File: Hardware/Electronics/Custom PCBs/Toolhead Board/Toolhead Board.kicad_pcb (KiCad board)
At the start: 4 copper layers, 75 x 75 mm, 161 parts, among them J1 USB C Receptacle, J2 Conn_02x04_Odd_Even, J3 Conn_02x08_Odd_Even, J4 Conn_02x08_Odd_Even, J5 Conn_02x08_Odd_Even, J6 Conn_02x04_Odd_Even, J7 Conn_01x02, J8 Conn_01x02, J9 120TR, Q1 MMBT4403, Q2 MMBT4403, Q3 MMBT4403, SW1 BOOT, SW2 RESET, U1 LF15_TO220, U10 BMI270, U11 G20N06D52, U12 G20N06D52, U13 PCA9685BS, U2 LF15_TO220, U3 RP2040, U4 W25Q128JVS, U5 SN65HVD1050D, U6 TMC2209-LA, U7 HX711, U8 HX711, U9 HX711, Y1 12MHz/12pF/50Ω/20ppm

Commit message: Update base mounting
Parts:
- C16: moved to B.Cu
- moved C5 99.6 mm to (75.2, 120.5), turned to -90 degrees
- moved C8 98.8 mm to (71.5, 122.9)
- moved C7 95.5 mm to (72.1, 116.0)
- moved C10 95.0 mm to (81.4, 118.3)
- moved C11 95.0 mm to (81.4, 120.8)
- moved C12 95.0 mm to (81.4, 123.3)
- moved C13 95.0 mm to (85.7, 115.8)
- moved C14 95.0 mm to (85.7, 118.3)
- moved C15 95.0 mm to (85.7, 120.8)
- moved C9 95.0 mm to (81.4, 115.8)
- moved C6 93.8 mm to (76.3, 115.8)
- moved C20 92.4 mm to (66.4, 99.8), turned to -90 degrees
- moved C19 92.1 mm to (67.9, 99.8), turned to -90 degrees
- moved C2 87.8 mm to (46.0, 43.4)
- moved C3 87.8 mm to (46.0, 45.9)
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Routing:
- net GNDA: track 278.8 -> 145.2 mm
- net D7: track 0.00 -> 26.9 mm
- net D0: track 0.00 -> 25.6 mm
- net D8: track 0.00 -> 24.9 mm
- net D1: track 0.00 -> 23.0 mm
- net SCL: track 1.94 -> 24.1 mm
- net SDA: track 1.61 -> 21.7 mm
- net /Microcontroller/RUN: track 0.00 -> 12.0 mm, vias 0 -> 2
- net +3.3V: track 66.9 -> 73.6 mm
- net V_MOT: track 40.1 -> 43.0 mm
- net MOT_DIAG: track 20.7 -> 21.0 mm, vias 1 -> 0

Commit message: Update layout slightly
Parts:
- C23, CR1: moved to B.Cu
- J7: footprint Connector_JST:JST_XH_B2B-XH-AM_1x02_P2.50mm_Vertical -> Connector_JST:JST_PH_B2B-PH-K_1x02_P2.00mm_Vertical
- J8: footprint Connector_JST:JST_XH_B2B-XH-AM_1x02_P2.50mm_Vertical -> Connector_AMASS:AMASS_XT30U-F_1x02_P5.0mm_Vertical
- moved C26 54.4 mm to (99.7, 58.0), turned to -120 degrees
- moved R10 49.0 mm to (33.9, 72.4), turned to 0 degrees
- moved C23 47.7 mm to (34.4, 68.9), turned to -90 degrees
- moved U5 42.0 mm to (45.6, 69.0), turned to 168.5 degrees
- moved J8 12.7 mm to (45.7, 58.2), turned to -60 degrees
- moved CR1 11.2 mm to (46.1, 69.1), turned to -11.5 degrees
- moved C1 11.0 mm to (37.0, 65.3)
- moved R11 9.68 mm to (39.6, 56.4)
- moved TP5 8.59 mm to (117.5, 62.1)
- moved J9 8.21 mm to (37.2, 60.5)
- moved J7 2.41 mm to (40.9, 67.0), turned to -101.5 degrees
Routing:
- net V_MOT: track 43.0 -> 18.6 mm
- net CAN_H: track 19.6 -> 0.00 mm, vias 2 -> 1
- net STRAIN_SCK: track 0.00 -> 19.4 mm, vias 0 -> 2
- net +5V: track 14.2 -> 31.9 mm
- net +3.3V: track 73.6 -> 90.8 mm
- net CAN_RX: track 8.87 -> 0.00 mm
- net CAN_L: track 7.56 -> 0.00 mm
- net CAN_S: track 4.37 -> 0.00 mm, vias 1 -> 0
- net CAN_TX: track 4.32 -> 0.00 mm
- net Net-(J9-Pin_1): track 2.44 -> 0.00 mm
- net Net-(U5-VREF): track 1.56 -> 0.00 mm
- net Net-(U5-S): vias 1 -> 0

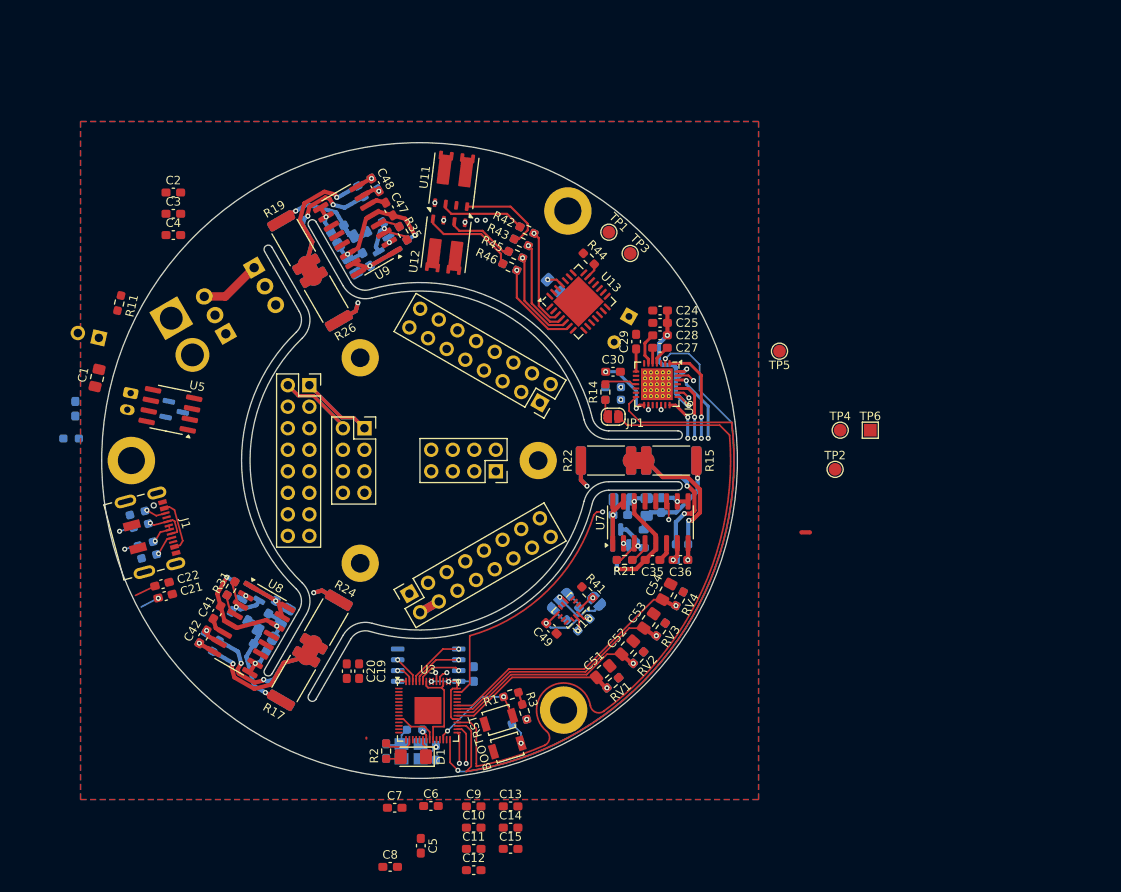
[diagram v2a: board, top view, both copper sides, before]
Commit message: Update toolhead schematic+layout and add tolerances to base
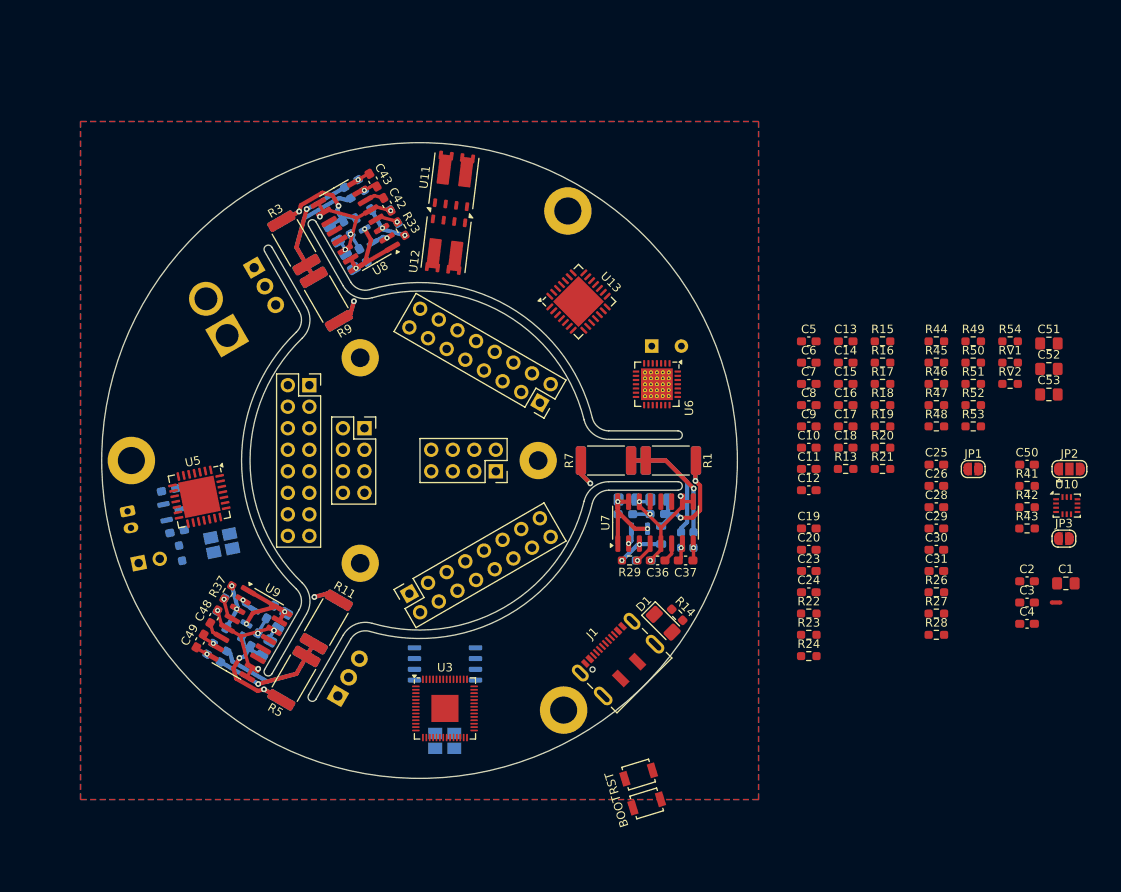
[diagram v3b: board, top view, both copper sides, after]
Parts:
- removed C54: 10u, Capacitor_SMD:C_0805_2012Metric_Pad1.18x1.45mm_HandSolder
- removed RV3, RV4: CG0603MLC-3.3LE, Resistor_SMD:R_0603_1608Metric_Pad0.98x0.95mm_HandSolder
- removed TP1, TP2, TP3, TP4, TP5: TestPoint, TestPoint:TestPoint_Pad_D1.5mm
- removed TP6: TestPoint, TestPoint:TestPoint_Pad_1.5x1.5mm
- added Y2: 16MHz/12pF, Oscillator:Oscillator_SMD_SeikoEpson_SG210-4Pin_2.5x2.0mm_HandSoldering, B.Cu at (51.7, 84.7)
- C16, C17, C18, JP2, JP3, R49, R50, R53, R54: moved to F.Cu
- C19: value 1u -> 100n
- C21, C22, C35, C41, C47: moved to B.Cu
- C23: value 100n -> 22p; moved to F.Cu
- C24: value 100n -> 22p
- C26: value 100u -> 100n; footprint Capacitor_THT:CP_Radial_D8.0mm_P3.50mm -> Capacitor_SMD:C_0603_1608Metric_Pad1.08x0.95mm_HandSolder; moved to F.Cu
- C27: value 22n -> 100u; footprint Capacitor_SMD:C_0603_1608Metric_Pad1.08x0.95mm_HandSolder -> Capacitor_THT:CP_Radial_D8.0mm_P3.50mm; moved to B.Cu
- C28: value 100n -> 22n
- C29: value 4.7u -> 100n
- C30: value 100n -> 4.7u
- C31: value 10uF -> 100n; footprint Capacitor_SMD:C_0805_2012Metric_Pad1.18x1.45mm_HandSolder -> Capacitor_SMD:C_0603_1608Metric_Pad1.08x0.95mm_HandSolder; moved to F.Cu
- C32, C34, C38, C40, C44, C46: value 0.1uF -> 10uF; footprint Capacitor_SMD:C_0603_1608Metric_Pad1.08x0.95mm_HandSolder -> Capacitor_SMD:C_0805_2012Metric_Pad1.18x1.45mm_HandSolder
- C33, C39, C45: value 10uF -> 0.1uF; footprint Capacitor_SMD:C_0805_2012Metric_Pad1.18x1.45mm_HandSolder -> Capacitor_SMD:C_0603_1608Metric_Pad1.08x0.95mm_HandSolder
- C37, C43: value 10uF -> 0.1uF; footprint Capacitor_SMD:C_0805_2012Metric_Pad1.18x1.45mm_HandSolder -> Capacitor_SMD:C_0603_1608Metric_Pad1.08x0.95mm_HandSolder; moved to F.Cu
- C49: value 100n -> 0.1uF
- C50: value 10u -> 100n; footprint Capacitor_SMD:C_0805_2012Metric_Pad1.18x1.45mm_HandSolder -> Capacitor_SMD:C_0603_1608Metric_Pad1.08x0.95mm_HandSolder; moved to F.Cu
- J8: footprint Connector_AMASS:AMASS_XT30U-F_1x02_P5.0mm_Vertical -> Connector_PinHeader_2.54mm:PinHeader_1x02_P2.54mm_Vertical
- J9: value 120TR -> Conn_01x02; footprint Connector_PinHeader_2.54mm:PinHeader_1x02_P2.54mm_Vertical -> Connector_AMASS:AMASS_XT30U-F_1x02_P5.0mm_Vertical
- R1, R3: value 10k -> 330; footprint Resistor_SMD:R_0603_1608Metric_Pad0.98x0.95mm_HandSolder -> Resistor_SMD:R_2512_6332Metric
- R10: value NC -> 330; footprint Resistor_SMD:R_0603_1608Metric_Pad0.98x0.95mm_HandSolder -> Resistor_SMD:R_2512_6332Metric
- R11: value 120 -> 330; footprint Resistor_SMD:R_0603_1608Metric_Pad0.98x0.95mm_HandSolder -> Resistor_SMD:R_2512_6332Metric
- R12: value 0R11 -> 330; footprint Resistor_SMD:R_0603_1608Metric_Pad0.98x0.95mm_HandSolder -> Resistor_SMD:R_2512_6332Metric
- R13: value 0R11 -> 10k; moved to F.Cu
- R14, R43, R46: value 100 -> 10k
- R15, R22, R24: value 330 -> 10k; footprint Resistor_SMD:R_2512_6332Metric -> Resistor_SMD:R_0603_1608Metric_Pad0.98x0.95mm_HandSolder
- R16: value 330 -> 1k; footprint Resistor_SMD:R_2512_6332Metric -> Resistor_SMD:R_0603_1608Metric_Pad0.98x0.95mm_HandSolder; moved to F.Cu
- R17: value 330 -> 1k; footprint Resistor_SMD:R_2512_6332Metric -> Resistor_SMD:R_0603_1608Metric_Pad0.98x0.95mm_HandSolder
- R18: value 330 -> 5.1k; footprint Resistor_SMD:R_2512_6332Metric -> Resistor_SMD:R_0603_1608Metric_Pad0.98x0.95mm_HandSolder; moved to F.Cu
- R19: value 330 -> 5.1k; footprint Resistor_SMD:R_2512_6332Metric -> Resistor_SMD:R_0603_1608Metric_Pad0.98x0.95mm_HandSolder
- R2: value 10k -> 330; footprint Resistor_SMD:R_0603_1608Metric_Pad0.98x0.95mm_HandSolder -> Resistor_SMD:R_2512_6332Metric; moved to B.Cu
- R20: value 330 -> 27.4; footprint Resistor_SMD:R_2512_6332Metric -> Resistor_SMD:R_0603_1608Metric_Pad0.98x0.95mm_HandSolder; moved to F.Cu
- R21: value 10k -> 27.4
- R23: value 330 -> 10k; footprint Resistor_SMD:R_2512_6332Metric -> Resistor_SMD:R_0603_1608Metric_Pad0.98x0.95mm_HandSolder; moved to F.Cu
- R25: value 330 -> 120; footprint Resistor_SMD:R_2512_6332Metric -> Resistor_SMD:R_0603_1608Metric_Pad0.98x0.95mm_HandSolder
- R26: value 330 -> 0R11; footprint Resistor_SMD:R_2512_6332Metric -> Resistor_SMD:R_0603_1608Metric_Pad0.98x0.95mm_HandSolder
- R27: value 330 -> 0R11; footprint Resistor_SMD:R_2512_6332Metric -> Resistor_SMD:R_0603_1608Metric_Pad0.98x0.95mm_HandSolder; moved to F.Cu
- R28: value 8.2k -> 100; moved to F.Cu
- R29, R33, R37: value 100 -> 10k; moved to F.Cu
- R30, R34, R38: value 100 -> 8.2k
- R31, R35: value 10k -> 100; moved to B.Cu
- R32, R36: value 8.2k -> 100
- R39, R40: value 2.2k -> 100
- R4: value 1k -> 330; footprint Resistor_SMD:R_0603_1608Metric_Pad0.98x0.95mm_HandSolder -> Resistor_SMD:R_2512_6332Metric
- R41: value 10k -> 2.2k
- R42: value 100 -> 2.2k
- R44: value 10k -> 100
- R47, R48: value 10k -> 100; moved to F.Cu
- R5: value 1k -> 330; footprint Resistor_SMD:R_0603_1608Metric_Pad0.98x0.95mm_HandSolder -> Resistor_SMD:R_2512_6332Metric; moved to F.Cu
- R51, R52: value 2.2k -> 10k; moved to F.Cu
- R6: value 5.1k -> 330; footprint Resistor_SMD:R_0603_1608Metric_Pad0.98x0.95mm_HandSolder -> Resistor_SMD:R_2512_6332Metric
- R7: value 5.1k -> 330; footprint Resistor_SMD:R_0603_1608Metric_Pad0.98x0.95mm_HandSolder -> Resistor_SMD:R_2512_6332Metric; moved to F.Cu
- R8: value 27.4 -> 330; footprint Resistor_SMD:R_0603_1608Metric_Pad0.98x0.95mm_HandSolder -> Resistor_SMD:R_2512_6332Metric
- R9: value 27.4 -> 330; footprint Resistor_SMD:R_0603_1608Metric_Pad0.98x0.95mm_HandSolder -> Resistor_SMD:R_2512_6332Metric; moved to F.Cu
- U5: value SN65HVD1050D -> MCP25625-x-SS; footprint Package_SO:SOIC-8_3.9x4.9mm_P1.27mm -> Package_DFN_QFN:QFN-28-1EP_6x6mm_P0.65mm_EP4.25x4.25mm
- moved C1 116.8 mm to (151.3, 89.5), turned to 0 degrees
- moved C2 110.7 mm to (146.7, 89.2)
- moved C3 110.7 mm to (146.7, 91.8)
- moved C4 110.7 mm to (146.7, 94.3)
- moved C23 88.6 mm to (120.9, 88.0), turned to 0 degrees
- moved R27 81.0 mm to (136.0, 93.1), turned to 0 degrees
- moved R26 79.9 mm to (136.0, 90.5), turned to 0 degrees
- moved R17 77.7 mm to (129.6, 66.0), turned to 0 degrees
- moved R18 76.6 mm to (129.6, 68.5), turned to 0 degrees
- moved C5 75.1 mm to (120.9, 60.9), turned to 0 degrees
- moved R20 73.6 mm to (129.6, 73.5), turned to 0 degrees
- moved C8 73.5 mm to (120.9, 68.5)
- moved R19 72.8 mm to (129.6, 71.0), turned to 0 degrees
- moved C7 69.9 mm to (120.9, 66.0)
- moved C6 68.7 mm to (120.9, 63.4)
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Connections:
- C19 pad 2: +5V -> +3.3V
- C20 pad 1: GND -> +5V
- C20 pad 2: +5V -> GND
- C23 pad 1: Net-(U5-VREF) -> GND
- C23 pad 2: GND -> Net-(U5-OSC2)
- C24 pad 1: V_MOT -> Net-(U5-OSC1)
- C27 pad 1: Net-(U6-CPI) -> V_MOT
- C27 pad 2: Net-(U6-CPO) -> GND
- C28 pad 1: V_MOT -> Net-(U6-CPI)
- C28 pad 2: Net-(U6-VCP) -> Net-(U6-CPO)
- C29 pad 1: GND -> V_MOT
- C29 pad 2: Net-(U6-5VOUT) -> Net-(U6-VCP)
- C30 pad 1: +3.3V -> GND
- C30 pad 2: GND -> Net-(U6-5VOUT)
- C31 pad 2: GNDA -> GND
- C32 pad 2: GNDA -> STRAIN1_E-
- C33 pad 1: /Load Cell Amplifiers/STRAIN1_E+ -> +3.3V
- C33 pad 2: GNDA -> STRAIN1_E-
- C34 pad 1: /Load Cell Amplifiers/STRAIN1_E+ -> STRAIN1_E+
- C34 pad 2: GNDA -> STRAIN1_E-
- C35 pad 1: GNDA -> STRAIN1_E+
- C35 pad 2: Net-(U7-VBG) -> STRAIN1_E-
- C36 pad 1: Net-(U7-INA+) -> STRAIN1_E-
- C36 pad 2: Net-(U7-INA-) -> Net-(U7-VBG)
- C37 pad 1: +3.3V -> Net-(U7-INA+)
- C37 pad 2: GNDA -> Net-(U7-INA-)
- C38 pad 2: GNDA -> STRAIN1_E-
- C39 pad 1: /Load Cell Amplifiers/STRAIN2_E+ -> +3.3V
- C39 pad 2: GNDA -> STRAIN1_E-
- C40 pad 1: /Load Cell Amplifiers/STRAIN2_E+ -> STRAIN2_E+
- C40 pad 2: GNDA -> STRAIN1_E-
- C41 pad 1: GNDA -> STRAIN2_E+
- C41 pad 2: Net-(U8-VBG) -> STRAIN1_E-
- C42 pad 1: Net-(U8-INA+) -> STRAIN1_E-
- C42 pad 2: Net-(U8-INA-) -> Net-(U8-VBG)
- C43 pad 1: +3.3V -> Net-(U8-INA+)
- C43 pad 2: GNDA -> Net-(U8-INA-)
- C44 pad 2: GNDA -> STRAIN1_E-
- C45 pad 1: /Load Cell Amplifiers/STRAIN3_E+ -> +3.3V
- C45 pad 2: GNDA -> STRAIN1_E-
- C46 pad 1: /Load Cell Amplifiers/STRAIN3_E+ -> STRAIN3_E+
- C46 pad 2: GNDA -> STRAIN1_E-
- C47 pad 1: GNDA -> STRAIN3_E+
- C47 pad 2: Net-(U9-VBG) -> STRAIN1_E-
- C48 pad 1: Net-(U9-INA+) -> STRAIN1_E-
- C48 pad 2: Net-(U9-INA-) -> Net-(U9-VBG)
- C49 pad 1: +3.3V -> Net-(U9-INA+)
- C49 pad 2: GND -> Net-(U9-INA-)
- C50 pad 1: GND -> +3.3V
- C50 pad 2: +5V -> GND
- C51 pad 1: THERM0 -> GND
- C51 pad 2: GND -> +5V
- C52 pad 1: THERM1 -> THERM0
- C53 pad 1: THERM2 -> THERM1
- J2 pad 1: +3.3V -> V_MOT
- J2 pad 2: +5V -> GND
- J2 pad 4: V_MOT -> GND
- J2 pad 5: 24V_PWM0 -> V_MOT
- J2 pad 6: 24V_PWM1 -> GND
- J2 pad 7: 24V_PWM2 -> V_MOT
- J2 pad 8: 24V_PWM3 -> GND
- J3 pad 1: +3.3V -> GND
- J3 pad 10: GND -> SERVO3
- J3 pad 11: GND -> SERVO2
- J3 pad 12: GND -> SERVO4
- J3 pad 13: GND -> SCL
- J3 pad 14: GND -> SDA
- J3 pad 15: GND -> CAN_H
- J3 pad 16: GND -> CAN_L
- J3 pad 2: +5V -> GND
- J3 pad 3: D0 -> GND
- J3 pad 4: D7 -> GND
- J3 pad 5: D1 -> +5V
- J3 pad 6: D8 -> GND
- J3 pad 7: SDA -> +5V
- J3 pad 8: SCL -> GND
- J3 pad 9: GND -> SERVO1
- J4 pad 1: +3.3V -> SERVO5
- J4 pad 10: THERM3 -> 24V_PWM1
- J4 pad 11: GND -> 24V_PWM3
- J4 pad 12: GND -> 24V_PWM1
- J4 pad 13: GND -> V_MOT
- J4 pad 14: GND -> V_MOT
- J4 pad 15: GND -> V_MOT
- J4 pad 16: GND -> V_MOT
- J4 pad 3: V_MOT -> SERVO6
- J4 pad 4: THERM0 -> GND
- J4 pad 5: V_MOT -> 24V_PWM2
- J4 pad 6: THERM1 -> 24V_PWM0
- J4 pad 7: CAN_H -> 24V_PWM2
- J4 pad 8: THERM2 -> 24V_PWM0
- J4 pad 9: CAN_L -> 24V_PWM3
- J5 pad 1: +3.3V -> D24
- J5 pad 10: SERVO7 -> GND
- J5 pad 11: SERVO4 -> +3.3V
- J5 pad 12: SERVO8 -> GND
- J5 pad 13: GND -> ADC0
- J5 pad 14: GND -> ADC1
- J5 pad 15: GND -> THERM0
- J5 pad 16: GND -> THERM1
- J5 pad 2: +5V -> D20
- J5 pad 3: V_MOT -> D25
- J5 pad 4: +5V -> D21
- J5 pad 5: SERVO1 -> D1
- J5 pad 6: SERVO5 -> GND
- J5 pad 7: SERVO2 -> +5V
- J5 pad 8: SERVO6 -> GND
- J5 pad 9: SERVO3 -> +3.3V
- J6 pad 1: OA2 -> OB1
- J6 pad 2: OB1 -> OA2
- J6 pad 3: OA1 -> OB2
- J6 pad 4: OB2 -> OA1
- J6 pad 5: GND -> +5V
- J6 pad 6: GND -> +3.3V
- J6 pad 7: GND -> +5V
- J6 pad 8: GND -> +3.3V
- J8 pad 1: GND -> CAN_H
- J8 pad 2: V_MOT -> Net-(J8-Pin_2)
- J9 pad 1: Net-(J9-Pin_1) -> GND
- J9 pad 2: CAN_H -> V_MOT
- L1 pad 2: /Load Cell Amplifiers/STRAIN1_E+ -> STRAIN1_E+
- L2 pad 2: /Load Cell Amplifiers/STRAIN2_E+ -> STRAIN2_E+
- L3 pad 2: /Load Cell Amplifiers/STRAIN3_E+ -> STRAIN3_E+
- NT1 pad 1: GNDA -> STRAIN1_E-
- R1 pad 1: +3.3V -> STRAIN1_E+
- R1 pad 2: /Microcontroller/RUN -> STRAIN1_S+
- R10 pad 1: Net-(U5-S) -> STRAIN1_E-
- R10 pad 2: CAN_S -> STRAIN2_S-
- R11 pad 1: Net-(J9-Pin_1) -> STRAIN3_S+
- R11 pad 2: CAN_L -> STRAIN1_E-
- R12 pad 1: Net-(U6-BRB) -> STRAIN1_E-
- R12 pad 2: GND -> STRAIN3_S-
- R13 pad 1: GND -> +3.3V
- R13 pad 2: Net-(U6-BRA) -> /Microcontroller/RUN
- R14 pad 1: Net-(JP1-B) -> Net-(D1-A)
- R14 pad 2: Net-(U6-DIAG) -> /Microcontroller/LED
- R15 pad 1: /Load Cell Amplifiers/STRAIN1_E+ -> /Microcontroller/QSPI_SS
- R15 pad 2: /Load Cell Amplifiers/STRAIN1_S+ -> +3.3V
- R16 pad 1: /Load Cell Amplifiers/STRAIN1_S- -> /Microcontroller/~{USB_BOOT}
- R16 pad 2: /Load Cell Amplifiers/STRAIN1_E+ -> /Microcontroller/QSPI_SS
- R17 pad 1: /Load Cell Amplifiers/STRAIN2_E+ -> Net-(C18-Pad2)
- R17 pad 2: /Load Cell Amplifiers/STRAIN2_S+ -> Net-(U3-XOUT)
- R18 pad 1: /Load Cell Amplifiers/STRAIN2_S- -> Net-(J1-CC1)
- R18 pad 2: /Load Cell Amplifiers/STRAIN2_E+ -> GND
- R19 pad 1: /Load Cell Amplifiers/STRAIN3_E+ -> Net-(J1-CC2)
- R19 pad 2: /Load Cell Amplifiers/STRAIN3_S+ -> GND
- R2 pad 1: Net-(D1-A) -> STRAIN1_S-
- R2 pad 2: /Microcontroller/LED -> STRAIN1_E+
- R20 pad 1: /Load Cell Amplifiers/STRAIN3_S- -> Net-(J1-D--PadA7)
- R20 pad 2: /Load Cell Amplifiers/STRAIN3_E+ -> /Microcontroller/USB+
- R21 pad 1: Net-(Q1-C) -> /Microcontroller/USB-
- R21 pad 2: Net-(U7-VFB) -> Net-(J1-D+-PadA6)
- R22 pad 1: /Load Cell Amplifiers/STRAIN1_S+ -> GND
- R22 pad 2: GNDA -> CAN_STBY
- R23 pad 1: GNDA -> +3.3V
- R23 pad 2: /Load Cell Amplifiers/STRAIN1_S- -> CAN_CS
- R24 pad 1: /Load Cell Amplifiers/STRAIN2_S+ -> CAN_RST
- R24 pad 2: GNDA -> +3.3V
- R25 pad 1: GNDA -> Net-(J8-Pin_2)
- R25 pad 2: /Load Cell Amplifiers/STRAIN2_S- -> CAN_L
- R26 pad 1: /Load Cell Amplifiers/STRAIN3_S+ -> Net-(U6-BRB)
- R26 pad 2: GNDA -> GND
- R27 pad 1: GNDA -> GND
- R27 pad 2: /Load Cell Amplifiers/STRAIN3_S- -> Net-(U6-BRA)
- R28 pad 1: Net-(U7-VFB) -> Net-(JP1-B)
- R28 pad 2: GNDA -> Net-(U6-DIAG)
- R29 pad 1: Net-(U7-INA-) -> Net-(Q1-C)
- R29 pad 2: /Load Cell Amplifiers/STRAIN1_S- -> Net-(U7-VFB)
- R3 pad 1: /Microcontroller/QSPI_SS -> STRAIN2_E+
- R3 pad 2: +3.3V -> STRAIN2_S+
- R30 pad 1: /Load Cell Amplifiers/STRAIN1_S+ -> Net-(U7-VFB)
- R30 pad 2: Net-(U7-INA+) -> STRAIN1_E-
- R31 pad 1: Net-(Q2-C) -> Net-(U7-INA-)
- R31 pad 2: Net-(U8-VFB) -> STRAIN1_S-
- R32 pad 1: Net-(U8-VFB) -> STRAIN1_S+
- R32 pad 2: GNDA -> Net-(U7-INA+)
- R33 pad 1: Net-(U8-INA-) -> Net-(Q2-C)
- R33 pad 2: /Load Cell Amplifiers/STRAIN2_S- -> Net-(U8-VFB)
- R34 pad 1: /Load Cell Amplifiers/STRAIN2_S+ -> Net-(U8-VFB)
- R34 pad 2: Net-(U8-INA+) -> STRAIN1_E-
- R35 pad 1: Net-(Q3-C) -> Net-(U8-INA-)
- R35 pad 2: Net-(U9-VFB) -> STRAIN2_S-
- R36 pad 1: Net-(U9-VFB) -> STRAIN2_S+
- R36 pad 2: GNDA -> Net-(U8-INA+)
- R37 pad 1: Net-(U9-INA-) -> Net-(Q3-C)
- R37 pad 2: /Load Cell Amplifiers/STRAIN3_S- -> Net-(U9-VFB)
- R38 pad 1: /Load Cell Amplifiers/STRAIN3_S+ -> Net-(U9-VFB)
- R38 pad 2: Net-(U9-INA+) -> STRAIN1_E-
- R39 pad 1: Net-(JP2-B) -> Net-(U9-INA-)
- R39 pad 2: SDA -> STRAIN3_S-
- R4 pad 1: /Microcontroller/~{USB_BOOT} -> STRAIN2_S-
- R4 pad 2: /Microcontroller/QSPI_SS -> STRAIN2_E+
- R40 pad 1: Net-(JP2-A) -> STRAIN3_S+
- R40 pad 2: SCL -> Net-(U9-INA+)
- R41 pad 1: /Accelerometer/Address Selection -> Net-(JP2-B)
- R41 pad 2: GND -> SDA
- R42 pad 1: Net-(U13-LED0) -> Net-(JP2-A)
- R42 pad 2: Net-(U11-G1) -> SCL
- R43 pad 1: Net-(U13-LED1) -> /Accelerometer/Address Selection
- R43 pad 2: Net-(U11-G2) -> GND
- R44 pad 1: GND -> Net-(U13-LED0)
- R44 pad 2: Net-(U13-~{OE}) -> Net-(U11-G1)
- R45 pad 1: Net-(U13-LED2) -> Net-(U13-LED1)
- R45 pad 2: Net-(U12-G1) -> Net-(U11-G2)
- R46 pad 1: Net-(U13-LED3) -> GND
- R46 pad 2: Net-(U12-G2) -> Net-(U13-~{OE})
- R47 pad 1: GND -> Net-(U13-LED2)
- R47 pad 2: Net-(U13-LED3) -> Net-(U12-G1)
- R48 pad 1: GND -> Net-(U13-LED3)
- R48 pad 2: Net-(U13-LED2) -> Net-(U12-G2)
- R49 pad 2: Net-(U13-LED1) -> Net-(U13-LED3)
- R5 pad 1: Net-(C18-Pad2) -> STRAIN3_E+
- R5 pad 2: Net-(U3-XOUT) -> STRAIN3_S+
- R50 pad 2: Net-(U13-LED0) -> Net-(U13-LED2)
- R51 pad 1: +3.3V -> GND
- R51 pad 2: THERM0 -> Net-(U13-LED1)
- R52 pad 1: +3.3V -> GND
- R52 pad 2: THERM1 -> Net-(U13-LED0)
- R53 pad 2: THERM2 -> THERM0
- R54 pad 2: THERM3 -> THERM1
- R6 pad 1: Net-(J1-CC1) -> STRAIN3_S-
- R6 pad 2: GND -> STRAIN3_E+
- R7 pad 1: Net-(J1-CC2) -> STRAIN1_S+
- R7 pad 2: GND -> STRAIN1_E-
- R8 pad 1: Net-(J1-D--PadA7) -> STRAIN1_E-
- R8 pad 2: /Microcontroller/USB+ -> STRAIN1_S-
- R9 pad 1: /Microcontroller/USB- -> STRAIN2_S+
- R9 pad 2: Net-(J1-D+-PadA6) -> STRAIN1_E-
- U13 pad 10: unconnected-(U13-LED7-Pad10) -> SERVO4
- U13 pad 12: SERVO1 -> SERVO5
- U13 pad 13: SERVO2 -> SERVO6
- U13 pad 14: SERVO3 -> unconnected-(U13-LED10-Pad14)
- U13 pad 15: SERVO4 -> unconnected-(U13-LED11-Pad15)
- U13 pad 16: SERVO5 -> unconnected-(U13-LED12-Pad16)
- U13 pad 17: SERVO6 -> unconnected-(U13-LED13-Pad17)
- U13 pad 18: SERVO7 -> unconnected-(U13-LED14-Pad18)
- U13 pad 19: SERVO8 -> unconnected-(U13-LED15-Pad19)
- U13 pad 7: unconnected-(U13-LED4-Pad7) -> SERVO1
- U13 pad 8: unconnected-(U13-LED5-Pad8) -> SERVO2
- U13 pad 9: unconnected-(U13-LED6-Pad9) -> SERVO3
- U3 pad 11: D8 -> MISO
- U3 pad 12: D9 -> MOT_EN
- U3 pad 13: D10 -> MOT_STP
- U3 pad 14: D11 -> MOT_DIR
- U3 pad 15: D12 -> MOT_DIAG
- U3 pad 17: D14 -> SCK
- U3 pad 18: D15 -> MOSI
- U3 pad 2: D0 -> MOT_UART
- U3 pad 27: D16 -> CAN_STBY
- U3 pad 28: MOT_EN -> TX0RTS
- U3 pad 29: MOT_STP -> CAN_RST
- U3 pad 30: MOT_DIR -> CAN_CS
- U3 pad 31: MOT_UART -> D20
- U3 pad 32: MOT_DIAG -> D21
- U3 pad 34: THERM0 -> CAN_INT
- U3 pad 35: THERM1 -> RX0BF
- U3 pad 36: THERM2 -> D24
- U3 pad 37: THERM3 -> D25
- U3 pad 38: STRAIN1_DO -> ADC0
- U3 pad 39: STRAIN2_DO -> ADC1
- U3 pad 40: STRAIN3_DO -> THERM0
- U3 pad 41: STRAIN_SCK -> THERM1
- U3 pad 6: CAN_TX -> STRAIN1_DO
- U3 pad 7: CAN_RX -> STRAIN2_DO
- U3 pad 8: CAN_S -> STRAIN_SCK
- U3 pad 9: D7 -> STRAIN3_DO
- U5 pad 1: CAN_TX -> CAN_CS
- U5 pad 2: GND -> CAN_RST
- U5 pad 3: +5V -> +3.3V
- U5 pad 4: CAN_RX -> Net-(U5-TXD)
- U5 pad 5: Net-(U5-VREF) -> Net-(U5-RXD)
- U5 pad 6: CAN_L -> unconnected-(U5-CLKOUT-Pad6)
- U5 pad 7: CAN_H -> TX0RTS
- U5 pad 8: Net-(U5-S) -> unconnected-(U5-~{Tx1RTS}-Pad8)
- U7 pad 10: GNDA -> STRAIN1_E-
- U7 pad 14: GNDA -> STRAIN1_E-
- U7 pad 5: GNDA -> STRAIN1_E-
- U7 pad 9: GNDA -> STRAIN1_E-
- U8 pad 10: GNDA -> STRAIN1_E-
- U8 pad 14: GNDA -> STRAIN1_E-
- U8 pad 5: GNDA -> STRAIN1_E-
- U8 pad 9: GNDA -> STRAIN1_E-
- U9 pad 10: GNDA -> STRAIN1_E-
- U9 pad 14: GNDA -> STRAIN1_E-
- U9 pad 5: GNDA -> STRAIN1_E-
- U9 pad 9: GNDA -> STRAIN1_E-
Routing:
- net STRAIN1_E-: track 0.00 -> 211.5 mm, vias 0 -> 19
- net GNDA: track 145.2 -> 0.00 mm, vias 12 -> 0
- net +3.3V: track 90.8 -> 39.7 mm, vias 10 -> 6
- net OB2: track 40.4 -> 0.00 mm, vias 2 -> 0
- net OA1: track 39.0 -> 0.00 mm, vias 2 -> 0
- net OB1: track 35.8 -> 0.00 mm, vias 2 -> 0
- net +5V: track 31.9 -> 0.00 mm, vias 1 -> 0
- net THERM3: track 31.2 -> 0.00 mm, vias 1 -> 0
- net OA2: track 31.2 -> 0.00 mm, vias 2 -> 0
- net THERM2: track 27.7 -> 0.00 mm, vias 1 -> 0
- net D7: track 26.9 -> 0.00 mm
- net D0: track 25.6 -> 0.00 mm
- net D8: track 24.9 -> 0.00 mm
- net SCL: track 24.1 -> 0.00 mm, vias 1 -> 0
- net THERM1: track 24.0 -> 0.00 mm, vias 1 -> 0
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
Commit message: Update toolhead PCB layout
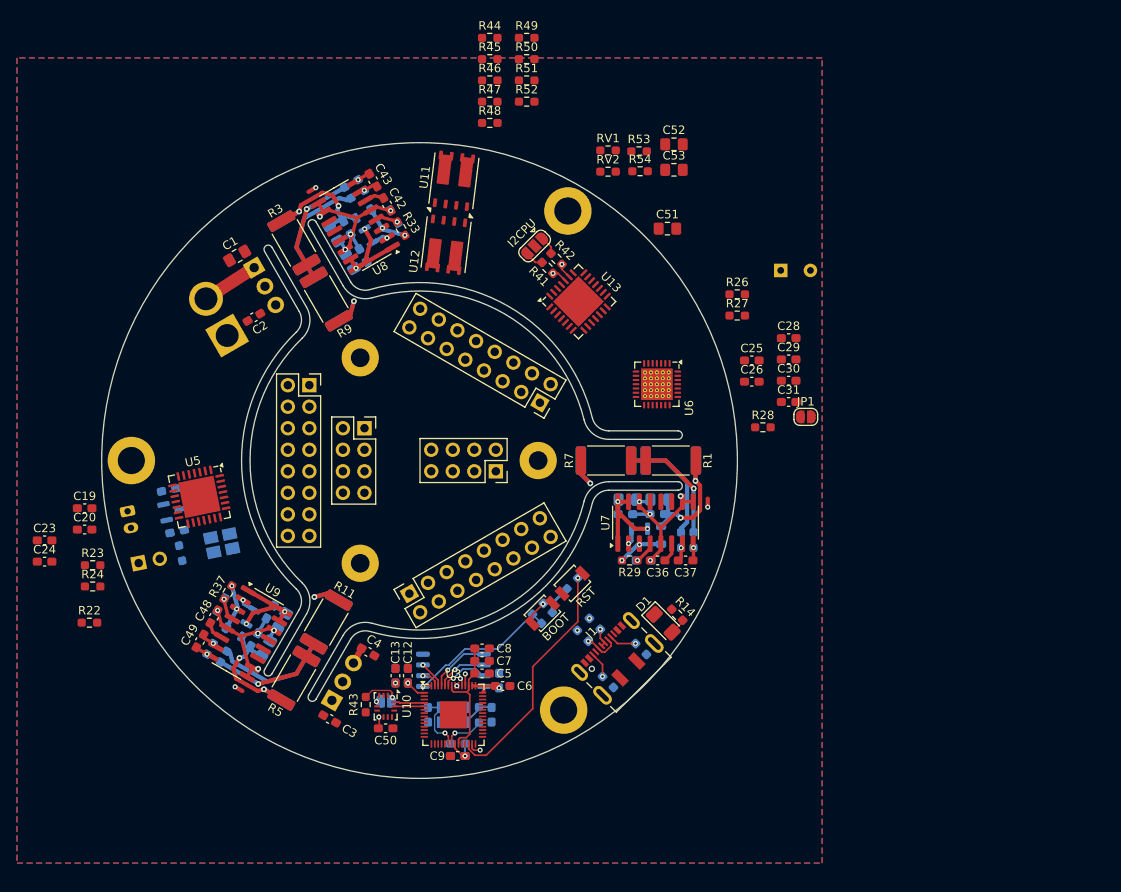
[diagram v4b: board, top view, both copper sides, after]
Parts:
- added NT2: NetTie_2, NetTie:NetTie-2_SMD_Pad0.5mm, F.Cu at (62.3, 43.1)
- added NT3: NetTie_2, NetTie:NetTie-2_SMD_Pad0.5mm, F.Cu at (53.7, 101.9)
- C10, C11, C14, C15, C16, C17, C18, JP3, R13, R15, R16, R17, R18, R19, R20, R21: moved to B.Cu
- moved C1 105.1 mm to (53.5, 50.9), turned to 30 degrees
- moved C2 96.4 mm to (55.5, 58.1), turned to -150 degrees
- moved C23 90.2 mm to (30.8, 84.4)
- moved C24 90.2 mm to (30.8, 86.9)
- moved C19 85.5 mm to (35.5, 80.6)
- moved C20 85.5 mm to (35.5, 83.1)
- moved R23 84.9 mm to (36.4, 87.3)
- moved R24 84.9 mm to (36.4, 89.9)
- moved R22 84.9 mm to (36.1, 94.1)
- moved U10 83.8 mm to (71.0, 104.0), turned to -90 degrees
- moved C3 83.4 mm to (64.4, 105.5), turned to -30 degrees
- moved JP3 82.3 mm to (71.0, 103.4)
- moved C50 81.8 mm to (71.0, 106.6)
- moved R43 80.7 mm to (68.7, 103.8), turned to -90 degrees
- moved C4 77.8 mm to (68.9, 97.6), turned to -30 degrees
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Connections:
- C38 pad 2: STRAIN1_E- -> STRAIN2_E-
- C39 pad 2: STRAIN1_E- -> STRAIN2_E-
- C40 pad 2: STRAIN1_E- -> STRAIN2_E-
- C41 pad 2: STRAIN1_E- -> STRAIN2_E-
- C42 pad 1: STRAIN1_E- -> STRAIN2_E-
- C44 pad 2: STRAIN1_E- -> STRAIN3_E-
- C45 pad 2: STRAIN1_E- -> STRAIN3_E-
- C46 pad 2: STRAIN1_E- -> STRAIN3_E-
- C47 pad 2: STRAIN1_E- -> STRAIN3_E-
- C48 pad 1: STRAIN1_E- -> STRAIN3_E-
- R10 pad 1: STRAIN1_E- -> STRAIN2_E-
- R11 pad 2: STRAIN1_E- -> STRAIN3_E-
- R12 pad 1: STRAIN1_E- -> STRAIN3_E-
- R34 pad 2: STRAIN1_E- -> STRAIN2_E-
- R38 pad 2: STRAIN1_E- -> STRAIN3_E-
- R9 pad 2: STRAIN1_E- -> STRAIN2_E-
- U8 pad 10: STRAIN1_E- -> STRAIN2_E-
- U8 pad 14: STRAIN1_E- -> STRAIN2_E-
- U8 pad 5: STRAIN1_E- -> STRAIN2_E-
- U8 pad 9: STRAIN1_E- -> STRAIN2_E-
- U9 pad 10: STRAIN1_E- -> STRAIN3_E-
- U9 pad 14: STRAIN1_E- -> STRAIN3_E-
- U9 pad 5: STRAIN1_E- -> STRAIN3_E-
- U9 pad 9: STRAIN1_E- -> STRAIN3_E-
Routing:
- net STRAIN1_E-: track 211.5 -> 74.2 mm, vias 19 -> 6
- net STRAIN2_E-: track 0.00 -> 74.2 mm, vias 0 -> 8
- net STRAIN3_E-: track 0.00 -> 74.2 mm, vias 0 -> 8
- net /Microcontroller/RUN: track 0.00 -> 29.1 mm, vias 0 -> 1
- net /Microcontroller/QSPI_SS: track 0.00 -> 19.0 mm, vias 0 -> 1
- net /Microcontroller/USB-: track 0.00 -> 18.9 mm, vias 0 -> 2
- net /Microcontroller/USB+: track 0.00 -> 17.1 mm, vias 0 -> 2
- net +3.3V: track 39.7 -> 56.4 mm, vias 6 -> 13
- net +1V1: track 0.00 -> 15.1 mm
- net Net-(U3-XIN): track 0.00 -> 7.94 mm, vias 0 -> 1
- net /Microcontroller/QSPI_SD0: track 0.00 -> 7.19 mm, vias 0 -> 1
- net V_MOT: track 0.00 -> 6.77 mm
- net /Microcontroller/QSPI_SCK: track 0.00 -> 6.02 mm, vias 0 -> 1
- net /Microcontroller/QSPI_SD3: track 0.00 -> 5.65 mm, vias 0 -> 1
- net SDA: track 0.00 -> 5.42 mm, vias 0 -> 1
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- added copper zone on In1.Cu, net +3.3V
- added copper zone on In2.Cu, net +5V
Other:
- board text added: "ACCEL ADDRSEL"
- board text added: "I2CPU"

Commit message: Update layout a bit more
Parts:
- C25, C26, C31, R22: moved to B.Cu
- moved JP1 24.0 mm to (96.8, 66.9), turned to 90 degrees
- moved C24 22.0 mm to (52.6, 84.6), turned to 101.5 degrees
- moved C30 20.7 mm to (97.8, 64.5)
- moved R24 20.2 mm to (48.8, 73.9), turned to 101.5 degrees
- moved C23 20.2 mm to (50.9, 84.9), turned to 101.5 degrees
- moved R23 19.5 mm to (50.3, 73.6), turned to -78.5 degrees
- moved C31 18.6 mm to (100.0, 69.8), turned to 180 degrees
- moved C29 18.1 mm to (100.5, 62.2)
- moved C27 17.9 mm to (101.3, 60.1), turned to 45 degrees
- moved R28 17.3 mm to (98.8, 66.9), turned to 90 degrees
- moved C26 17.1 mm to (97.5, 62.2), turned to -135 degrees
- moved C51 17.0 mm to (88.7, 54.6), turned to 45 degrees
- moved C25 15.7 mm to (98.5, 63.2), turned to -135 degrees
- moved C28 15.0 mm to (103.5, 61.2), turned to -90 degrees
- moved R22 14.8 mm to (48.2, 85.7), turned to 101.5 degrees
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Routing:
- net OB2: track 0.00 -> 39.1 mm, vias 0 -> 1
- net OA1: track 0.00 -> 33.9 mm, vias 0 -> 1
- net OB1: track 0.00 -> 33.7 mm, vias 0 -> 1
- net OA2: track 0.00 -> 30.5 mm, vias 0 -> 1
- net V_MOT: track 6.77 -> 24.1 mm, vias 0 -> 2
- net CAN_L: track 0.00 -> 17.1 mm, vias 0 -> 2
- net CAN_H: track 0.00 -> 14.4 mm, vias 0 -> 2
- net MOT_UART: track 0.00 -> 11.5 mm, vias 0 -> 1
- net GND: track 0.00 -> 9.27 mm, vias 0 -> 3
- net MOT_STP: track 0.00 -> 8.89 mm, vias 0 -> 1
- net +3.3V: track 56.4 -> 63.7 mm, vias 13 -> 17
- net MOT_DIR: track 0.00 -> 7.12 mm, vias 0 -> 1
- net VBUS: track 0.00 -> 6.25 mm, vias 0 -> 2
- net Net-(U5-TXD): track 0.00 -> 5.91 mm
- net Net-(U5-RXD): track 0.00 -> 5.56 mm, vias 0 -> 1
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
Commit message: Update layout
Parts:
- R52: moved to B.Cu
- moved R44 12.8 mm to (88.7, 36.7), turned to -90 degrees
- moved R52 4.22 mm to (88.7, 36.7), turned to 90 degrees
- moved R48 1.15 mm to (82.5, 36.0)
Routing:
- net V_MOT: track 24.1 -> 74.8 mm
- net GND: vias 3 -> 16
- added copper zone on In1.Cu, net GND
- added copper zone on In2.Cu, net GND

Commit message: Updated PCB
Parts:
- moved R46 26.4 mm to (96.9, 52.9), turned to 135 degrees
- moved R45 16.5 mm to (86.5, 43.8), turned to 83 degrees
- moved R50 16.2 mm to (84.5, 43.5), turned to -97 degrees
- moved R44 15.2 mm to (86.0, 51.7), turned to 135 degrees
- moved R52 15.2 mm to (86.0, 51.7), turned to -45 degrees
- moved R51 13.9 mm to (88.1, 44.0), turned to -97 degrees
- moved R47 10.7 mm to (82.8, 43.4), turned to -97 degrees
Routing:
- net Net-(U13-LED1): track 0.00 -> 21.9 mm
- net Net-(U13-LED0): track 0.00 -> 9.12 mm, vias 0 -> 1
- net Net-(U12-G1): track 0.00 -> 4.69 mm
- net Net-(U11-G2): track 0.00 -> 4.28 mm
- net Net-(U13-LED2): track 0.00 -> 2.60 mm
- net OB1: track 33.7 -> 35.9 mm
- net Net-(U13-~{OE}): track 0.00 -> 1.83 mm
- net OB2: track 39.1 -> 40.7 mm
- net OA1: track 33.9 -> 34.7 mm
- net OA2: track 30.5 -> 31.3 mm

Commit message: Updated PCB
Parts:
- moved R49 28.5 mm to (81.3, 52.9), turned to 83 degrees
- moved R48 17.1 mm to (82.9, 53.1), turned to 83 degrees
- moved C51 0.56 mm to (89.2, 54.2)
- moved R42 0.56 mm to (91.6, 50.9)
- moved R46 0.56 mm to (97.3, 52.5)
- moved U13 0.56 mm to (94.2, 55.9)
- moved R41 0.56 mm to (90.5, 51.9)
- moved R51 0.51 mm to (88.2, 44.5), turned to -115 degrees
- moved R45 0.30 mm to (86.8, 43.8), turned to 65 degrees
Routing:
- net Net-(U13-LED2): track 2.60 -> 25.1 mm
- net Net-(U13-LED3): track 0.00 -> 14.3 mm
- net Net-(U11-G2): track 4.28 -> 0.00 mm
- net Net-(U13-LED1): track 21.9 -> 19.7 mm
- net Net-(U13-~{OE}): track 1.83 -> 0.00 mm
